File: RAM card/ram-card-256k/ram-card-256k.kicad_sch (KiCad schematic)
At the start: 6 parts, among them U1 HC138, U2 KM681000BLG, U3 KM681000BLG

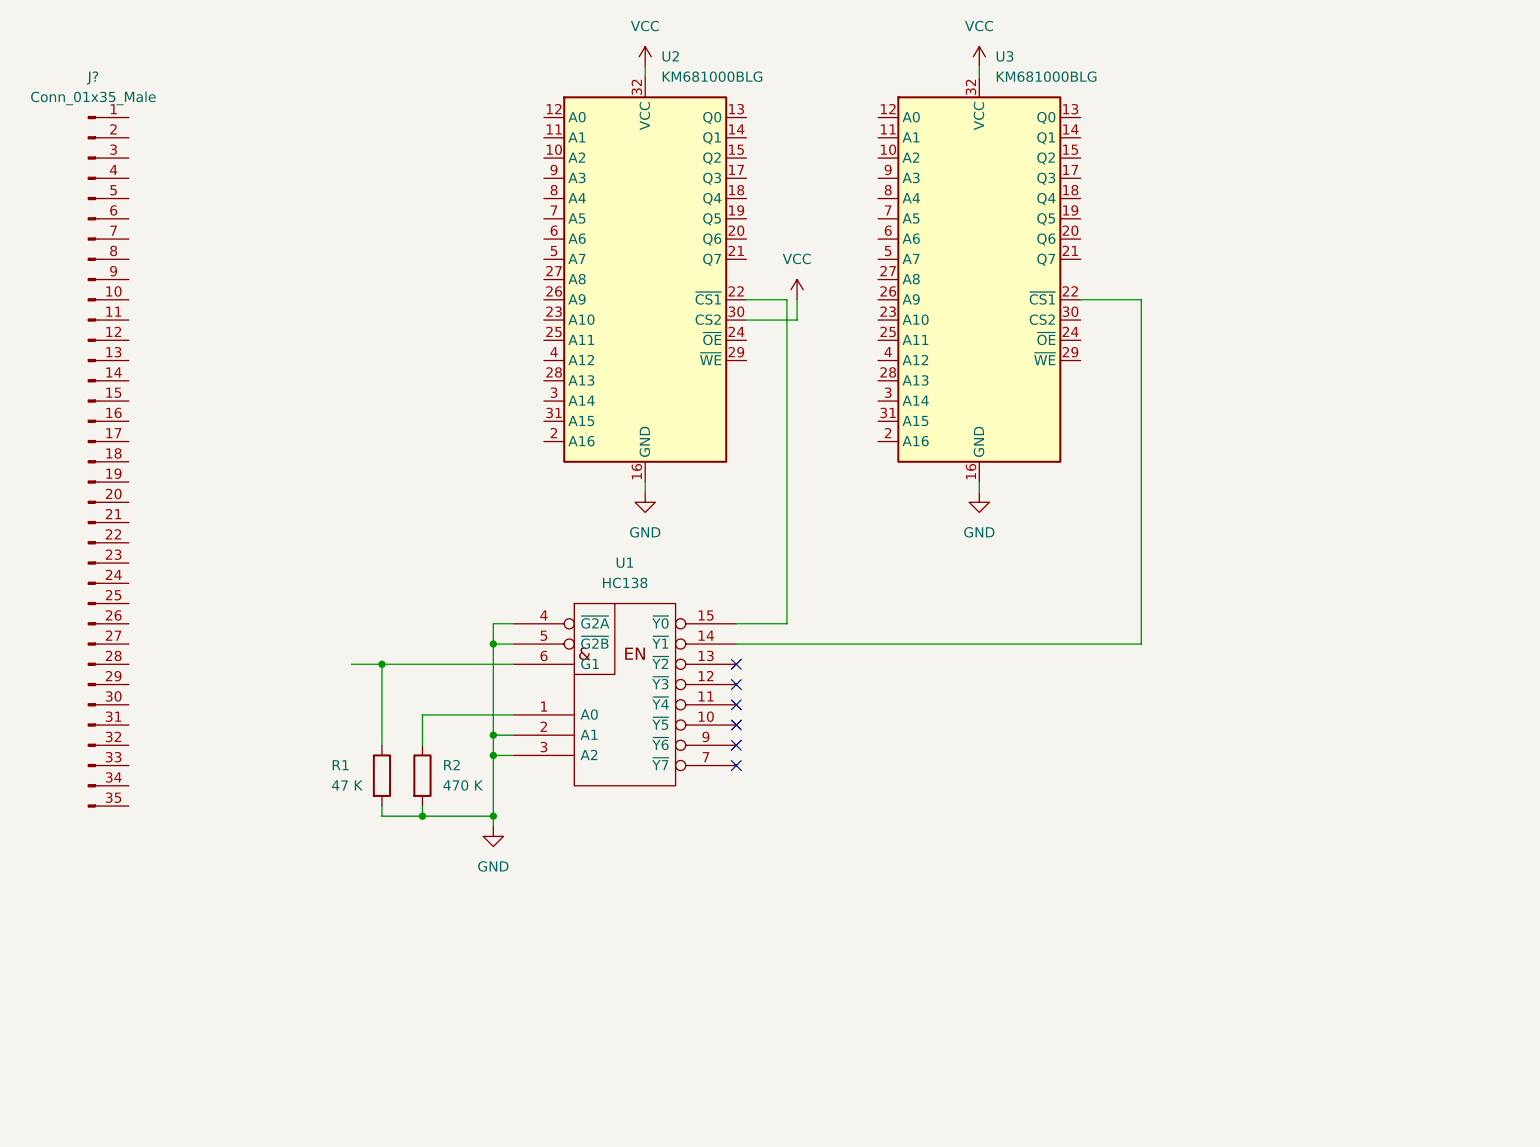
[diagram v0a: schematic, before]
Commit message: Design symbol for RAM card connector
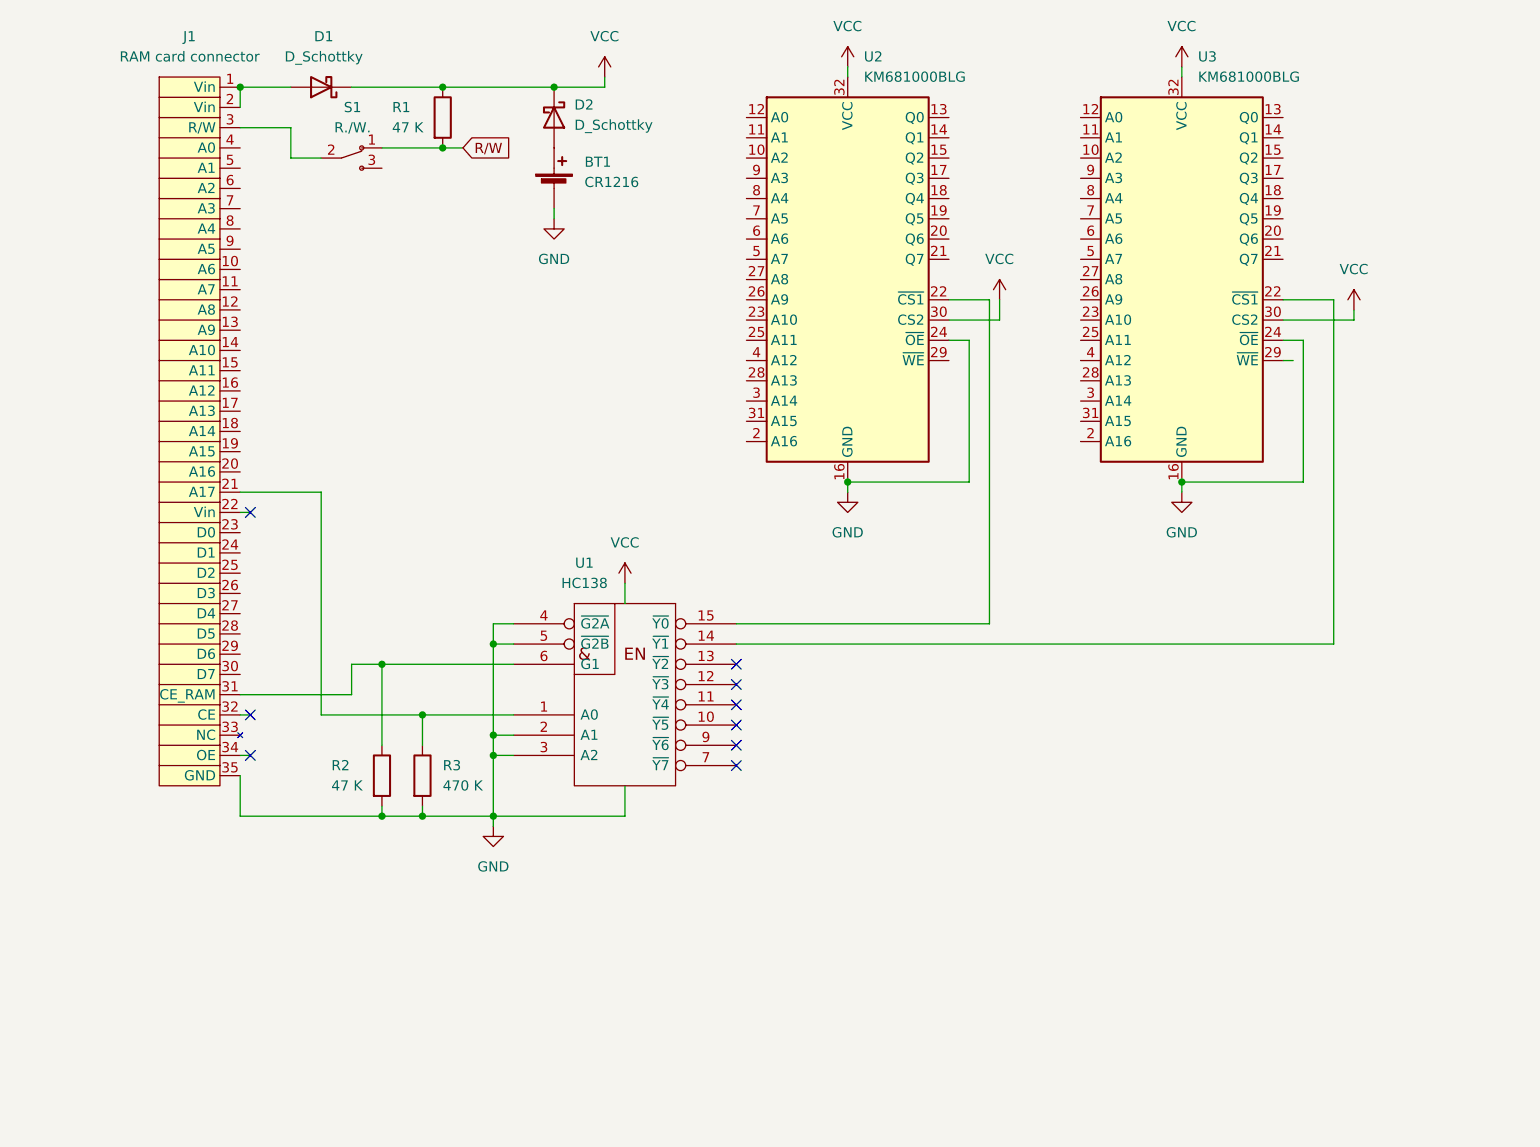
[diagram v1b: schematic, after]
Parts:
- removed J?: Conn_01x35_Male, symbol Connector:Conn_01x35_Male
- added BT1: CR1216, symbol Device:Battery_Cell
- added D1, D2: D_Schottky, symbol Device:D_Schottky
- added J1: RAM card connector, symbol custom-symbols:RAM_card_connector
- added R1: 47 K, symbol Device:R
- added S1: R./W., symbol custom-symbols:Slider_switch
- renumbered R1 to R2, R2 to R3
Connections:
- net GND: now also U2.24 (~{OE}), U3.24 (~{OE}), BT1.2 (-), J1.35 (GND)
- net VCC: now also U3.30 (CS2), D1.1 (K), D2.1 (K), R1.1
- net at R3.1, U1.1 (A0): now also J1.21 (A17)
- net at R2.1, U1.6 (G1): now also J1.31 (CE_RAM)
- new net: D1.2 (A), J1.1 (Vin), J1.2 (Vin)
- new net: J1.3 (R/W), S1.2
- new net: BT1.1 (+), D2.2 (A)
- new net R/W: R1.2, S1.1
- no-connect marks 6 -> 9
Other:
- moved on the sheet: U2, U3

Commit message: Add custom footprints
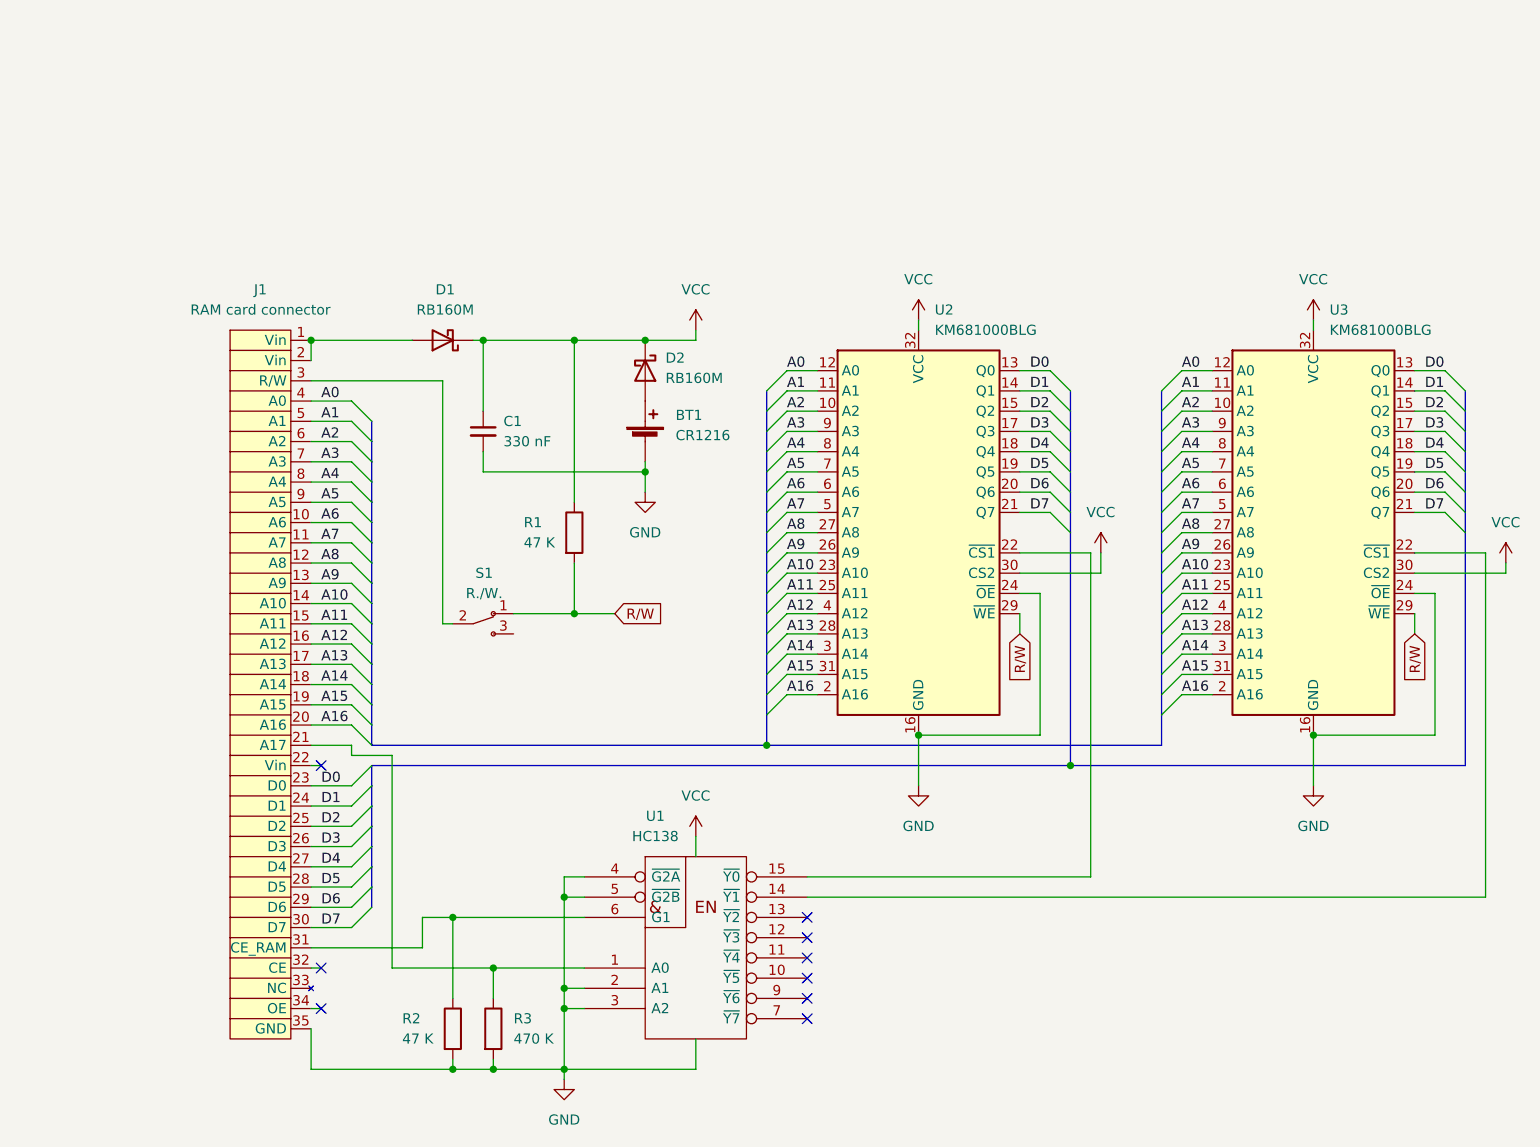
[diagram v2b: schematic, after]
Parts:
- added C1: 330 nF, Capacitor_SMD:C_1812_4532Metric, symbol Device:C_Small
- BT1: footprint (none) -> custom-footprints:Battery_CR1216
- D1, D2: value D_Schottky -> RB160M
- J1: footprint (none) -> custom-footprints:RAM_card_connector_35
- R1, R2, R3: footprint (none) -> Resistor_SMD:R_1206_3216Metric
- S1: footprint (none) -> custom-footprints:slider_switch_7x3
- U1: footprint (none) -> Package_SO:SOP-16_4.55x10.3mm_P1.27mm
- U2, U3: footprint (none) -> Package_SO:SSOP-32_11.305x20.495mm_P1.27mm
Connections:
- net GND: now also C1.2
- net R/W: now also U2.29 (~{WE}), U3.29 (~{WE})
- net VCC: now also C1.1
- net A2: now reaches U2.10 (A2)
- net A2: now also J1.6 (A2), U3.10 (A2)
- net A1: now reaches U2.11 (A1)
- net A1: now also J1.5 (A1), U3.11 (A1)
- net A0: now reaches U2.12 (A0)
- net A0: now also J1.4 (A0), U3.12 (A0)
- net D0: now reaches U2.13 (Q0)
- net D0: now also J1.23 (D0), U3.13 (Q0)
- net D1: now reaches U2.14 (Q1)
- net D1: now also J1.24 (D1), U3.14 (Q1)
- net D2: now reaches U2.15 (Q2)
- net D2: now also J1.25 (D2), U3.15 (Q2)
- net D3: now reaches U2.17 (Q3)
- net D3: now also J1.26 (D3), U3.17 (Q3)
- net D4: now reaches U2.18 (Q4)
- net D4: now also J1.27 (D4), U3.18 (Q4)
- net D5: now reaches U2.19 (Q5)
- net D5: now also J1.28 (D5), U3.19 (Q5)
- net A16: now reaches U2.2 (A16)
- net A16: now also J1.20 (A16), U3.2 (A16)
- net D6: now reaches U2.20 (Q6)
- net D6: now also J1.29 (D6), U3.20 (Q6)
- net D7: now reaches U2.21 (Q7)
- net D7: now also J1.30 (D7), U3.21 (Q7)
- net A10: now reaches U2.23 (A10)
- net A10: now also J1.14 (A10), U3.23 (A10)
- net A11: now reaches U2.25 (A11)
- net A11: now also J1.15 (A11), U3.25 (A11)
- net A9: now reaches U2.26 (A9)
- net A9: now also J1.13 (A9), U3.26 (A9)
- net A8: now reaches U2.27 (A8)
- net A8: now also J1.12 (A8), U3.27 (A8)
- net A13: now reaches U2.28 (A13)
- net A13: now also J1.17 (A13), U3.28 (A13)
- net A14: now reaches U2.3 (A14)
- net A14: now also J1.18 (A14), U3.3 (A14)
- net A15: now reaches U2.31 (A15)
- net A15: now also J1.19 (A15), U3.31 (A15)
- net A12: now reaches U2.4 (A12)
- net A12: now also J1.16 (A12), U3.4 (A12)
- net A7: now reaches U2.5 (A7)
- net A7: now also J1.11 (A7), U3.5 (A7)
- net A6: now reaches U2.6 (A6)
- net A6: now also J1.10 (A6), U3.6 (A6)
- net A5: now reaches U2.7 (A5)
- net A5: now also J1.9 (A5), U3.7 (A5)
- net A4: now reaches U2.8 (A4)
- net A4: now also J1.8 (A4), U3.8 (A4)
- net A3: now reaches U2.9 (A3)
- net A3: now also J1.7 (A3), U3.9 (A3)
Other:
- moved on the sheet: BT1, D1, D2, J1, R1, R2, R3, S1, U1, U2, U3

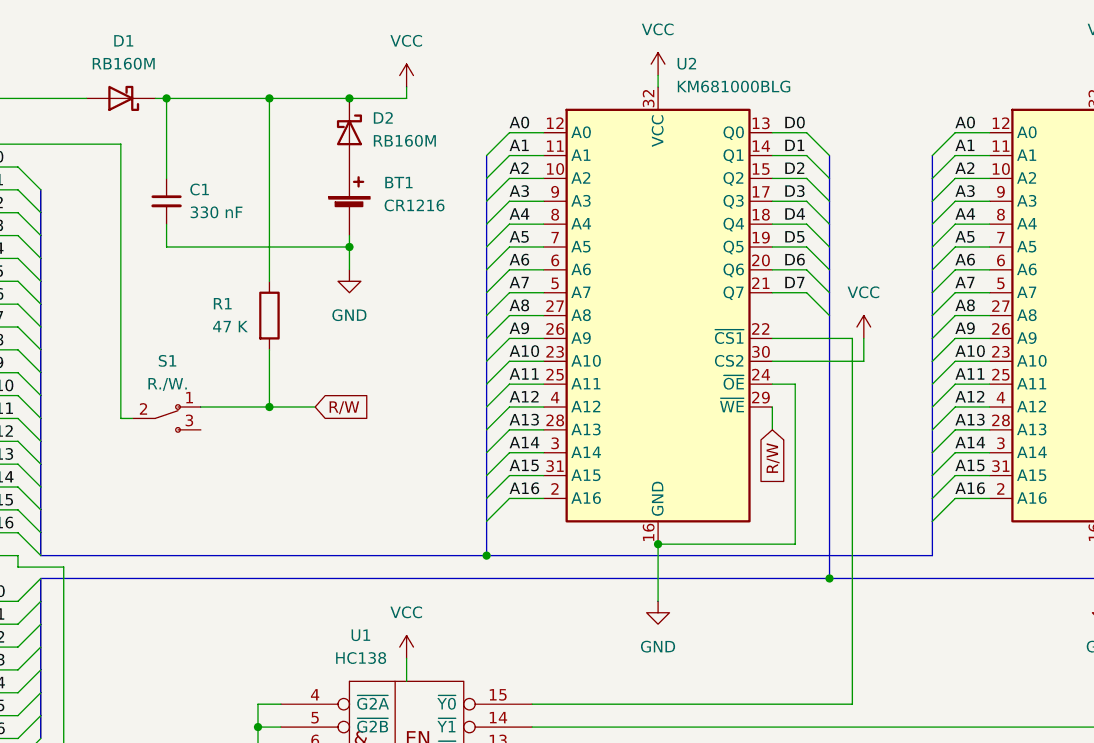
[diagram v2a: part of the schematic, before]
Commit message: Fix rules check errors
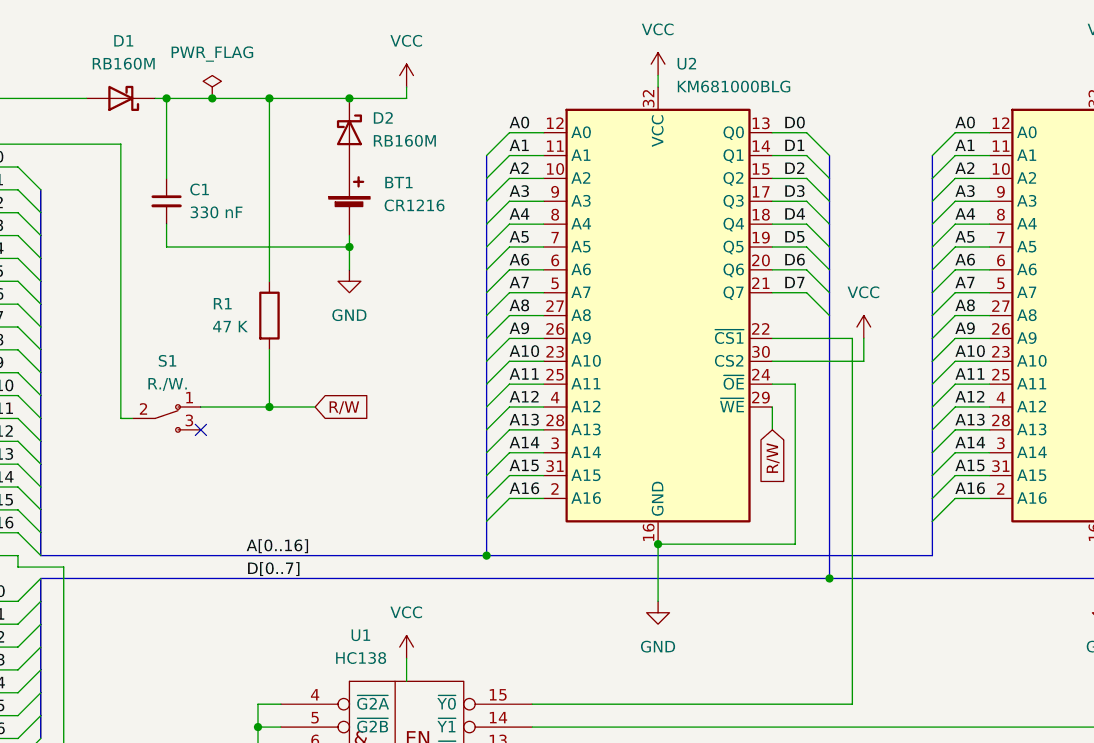
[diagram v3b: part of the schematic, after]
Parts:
- D1, D2: footprint (none) -> Diode_SMD:D_SOD-123
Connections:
- no-connect marks 9 -> 10
